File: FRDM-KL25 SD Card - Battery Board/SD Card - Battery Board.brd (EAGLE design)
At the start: 81.3 x 53.3 mm, 72 parts, among them J10 SSW-103-02-S-S, J11 SSW-102-02-S-S, J12 SSW-103-02-S-S, J13 SSW-103-02-S-S, J14 SSW-103-02-S-S, J3 SSW-108-02-S-D, J4 SSW-110-02-S-D, J5 SSW-108-02-S-D, J6 SSW-106-02-S-D, J7 SSW-102-02-S-S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

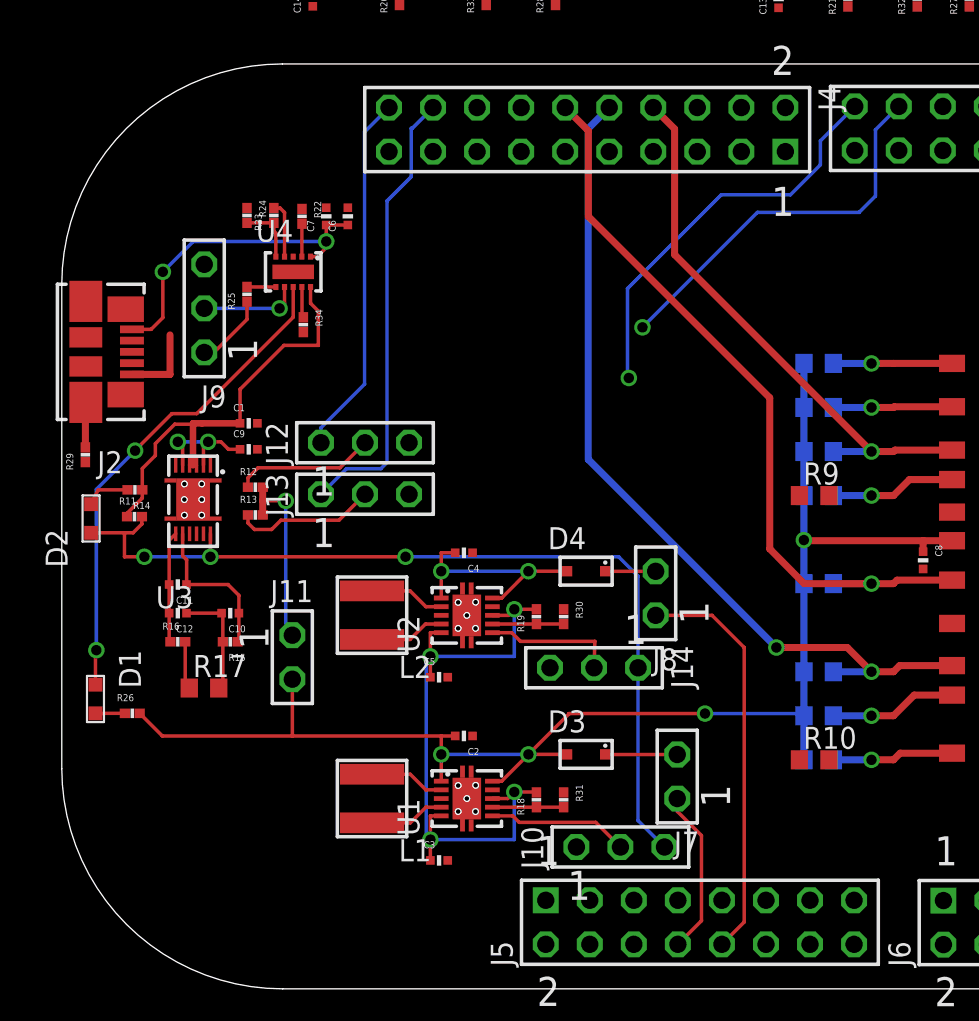
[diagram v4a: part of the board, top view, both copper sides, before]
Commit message: FRDM-KL25Z: Added a battery connector that uses a 1mm pitch. A few connections have been cleaned up to allow for better routing
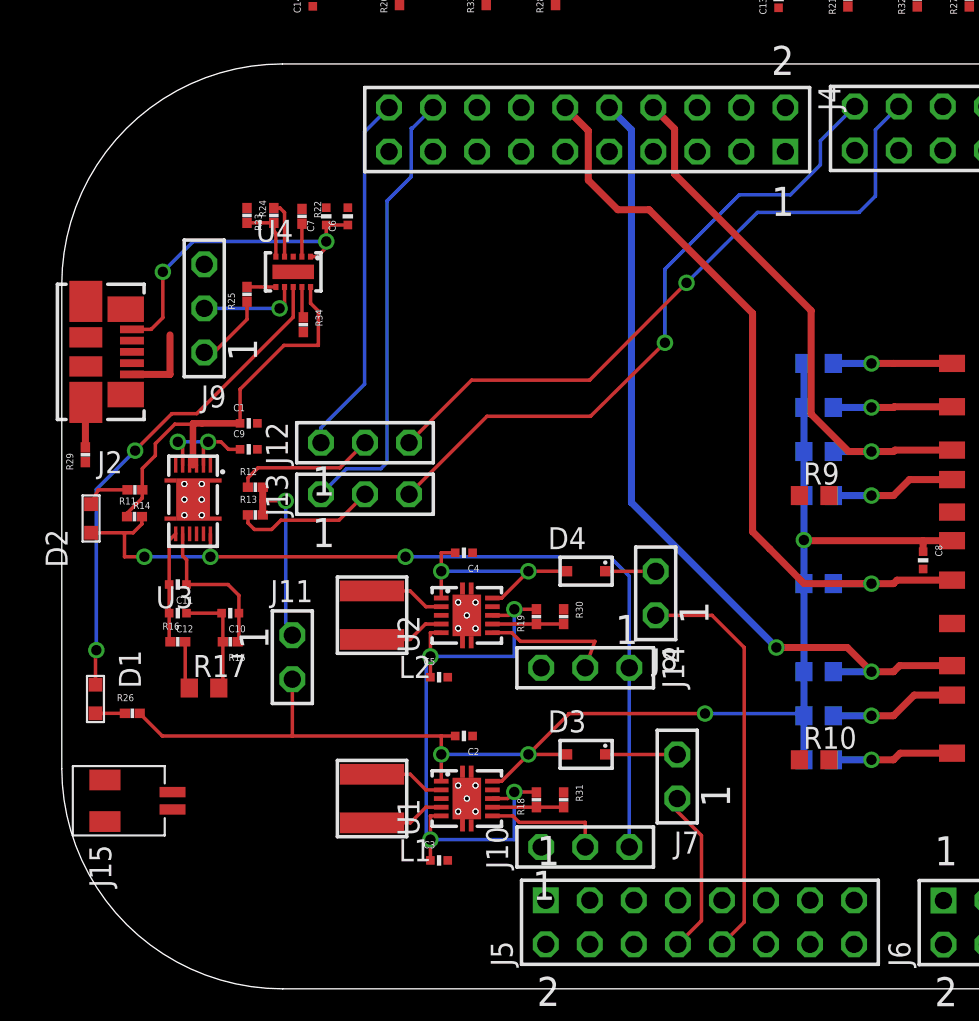
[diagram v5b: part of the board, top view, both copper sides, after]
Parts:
- added J15: 501568-0207-V2, Kas-Connectors:50156-0207
- moved J10 2.03 mm to (15.2, 5.36)
- moved J14 0.51 mm to (15.2, 15.7)
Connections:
- net PACK+: now also J15.P$1
- net PACK-: now also J15.P$2
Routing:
- net I2C-SCL-0: track 22.3 -> 38.5 mm
- net I2C-SDA-0: track 23.5 -> 38.3 mm
- net N$2: track 8.13 -> 6.93 mm
- net !BAT_LOW: track 52.6 -> 51.5 mm
- net SPI-SCLK-SD: track 44.0 -> 45.0 mm
- net SPI-MISO-SD: track 49.2 -> 48.2 mm
- net SPI-MOSI-SD: track 31.9 -> 32.7 mm

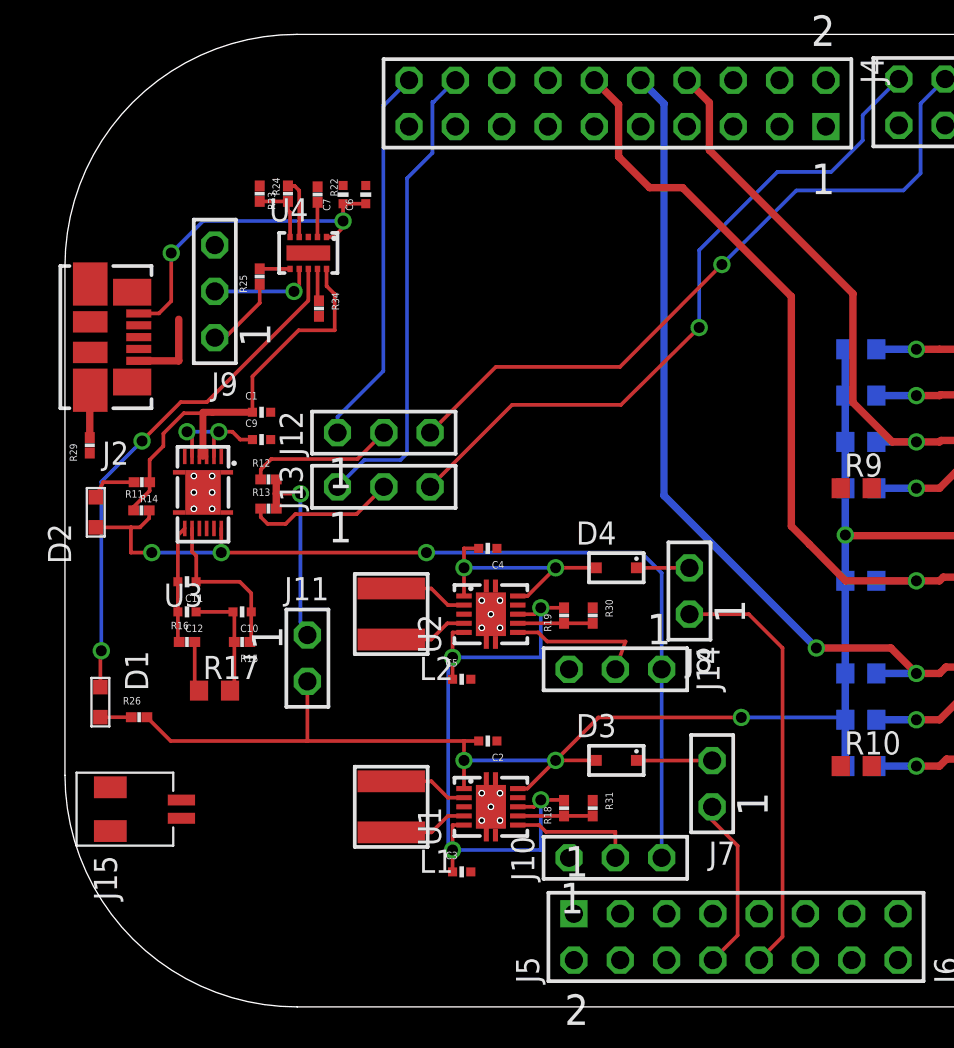
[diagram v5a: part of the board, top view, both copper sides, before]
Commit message: FRDM-KL25Z: All connections have been routed NOT cleanly. The board still needs cleaning up and this will hopefully be done before the next commit
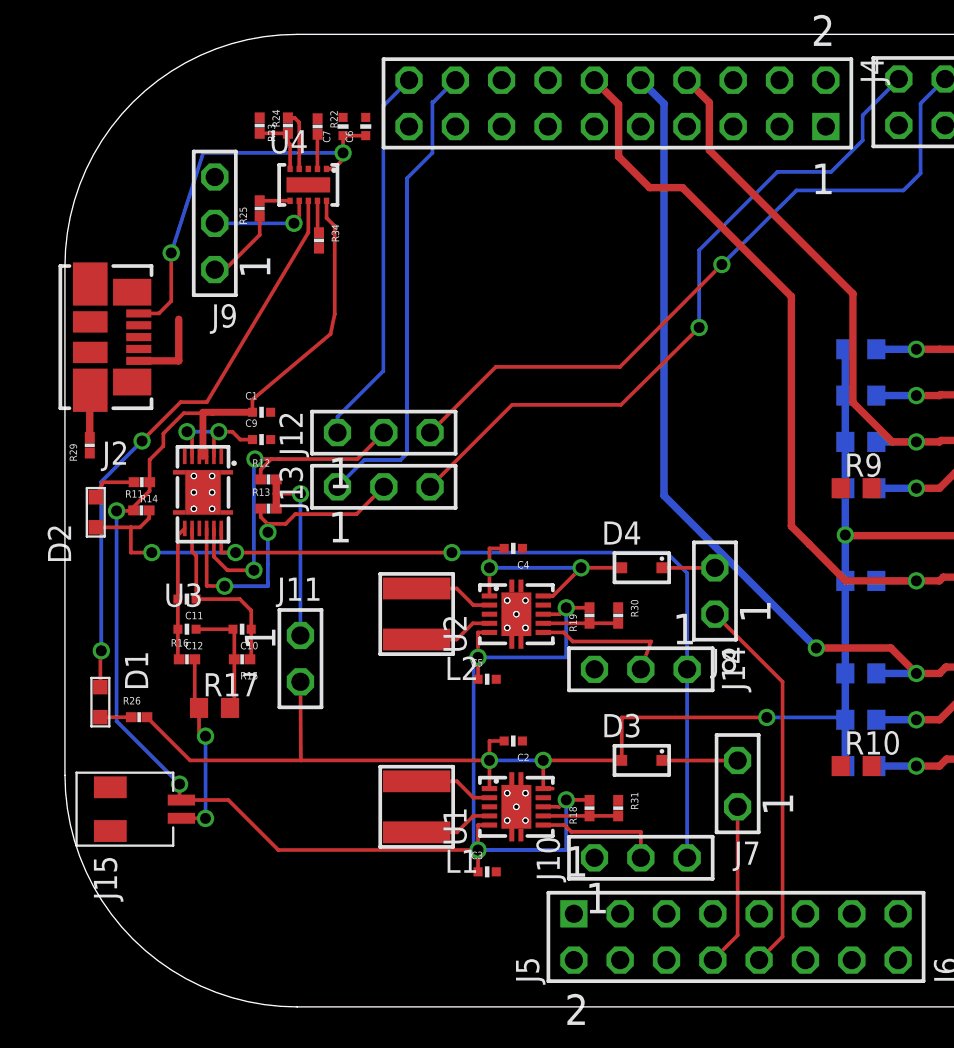
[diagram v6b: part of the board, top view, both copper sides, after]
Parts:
- moved C6 3.73 mm to (1.55, 45.5)
- moved C7 3.73 mm to (0.30, 45.5)
- moved J9 3.73 mm to (-6.73, 40.2)
- moved R22 3.73 mm to (-1.09, 45.5)
- moved R23 3.73 mm to (-2.72, 45.5)
- moved R24 3.73 mm to (-4.27, 45.5)
- moved U4 3.73 mm to (-1.60, 42.3)
- moved R25 3.73 mm to (-4.27, 41.0)
- moved R34 3.73 mm to (-1.02, 39.2)
- moved D3 1.40 mm to (16.7, 10.7)
- moved D4 1.40 mm to (16.7, 21.3)
- moved J8 1.40 mm to (20.7, 20.0)
- moved C2 1.40 mm to (9.64, 11.8)
- moved C3 1.40 mm to (8.21, 4.59)
- moved C4 1.40 mm to (9.64, 22.3)
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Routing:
- net PACK+: track 62.4 -> 100.8 mm, vias 4 -> 6
- net SCL: track 8.13 -> 19.2 mm, vias 0 -> 2
- net SDA: track 8.21 -> 18.1 mm, vias 0 -> 2
- net PACK-: track 2.76 -> 10.8 mm, vias 0 -> 2
- net +5V_CHARGE: track 18.5 -> 21.8 mm
- net !CHARGE: track 28.5 -> 31.5 mm
- net 5V_KL25Z: track 23.5 -> 21.0 mm
- net !BAT_LOW: track 51.5 -> 53.7 mm
- net N$6: track 6.46 -> 7.41 mm
- net N$7: track 9.06 -> 10.0 mm
- net 3.3V_KL25Z: track 9.55 -> 8.97 mm

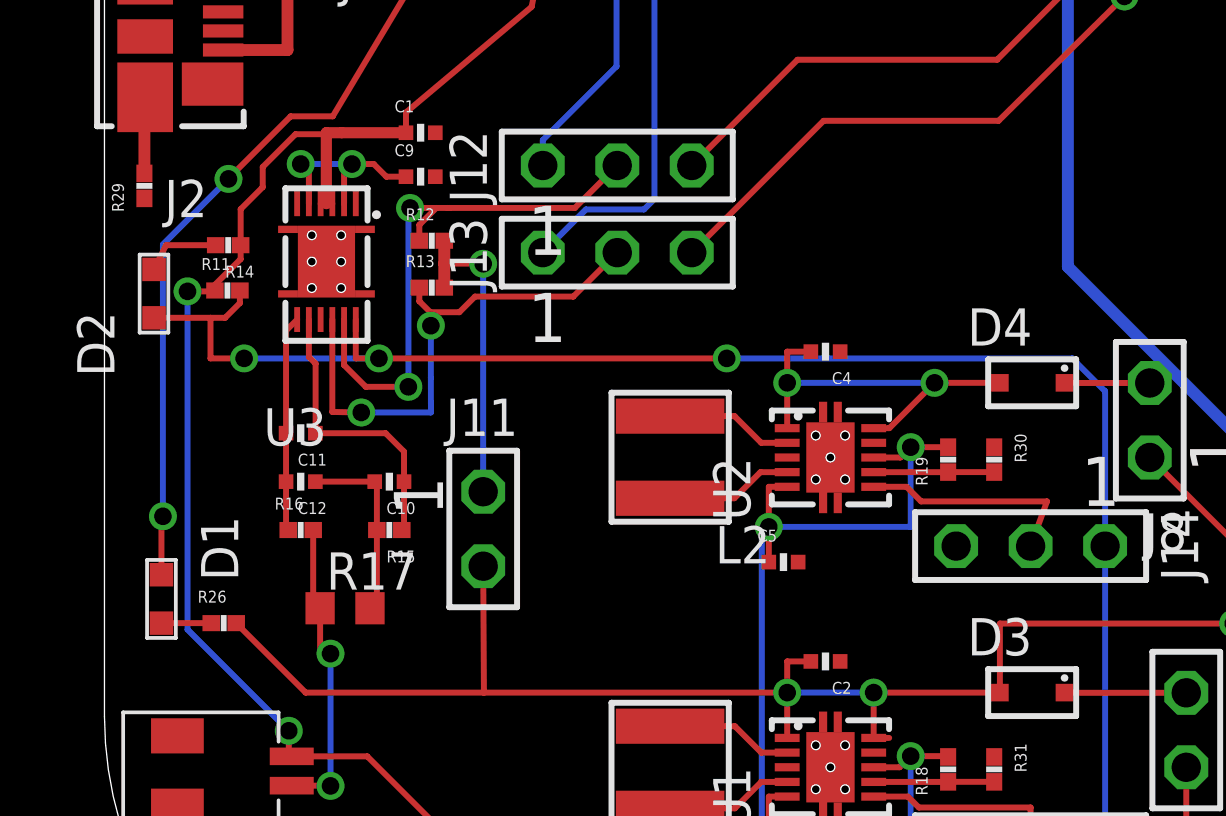
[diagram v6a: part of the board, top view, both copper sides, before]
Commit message: FRDM-KL25Z: Cleaned up a few routed connections
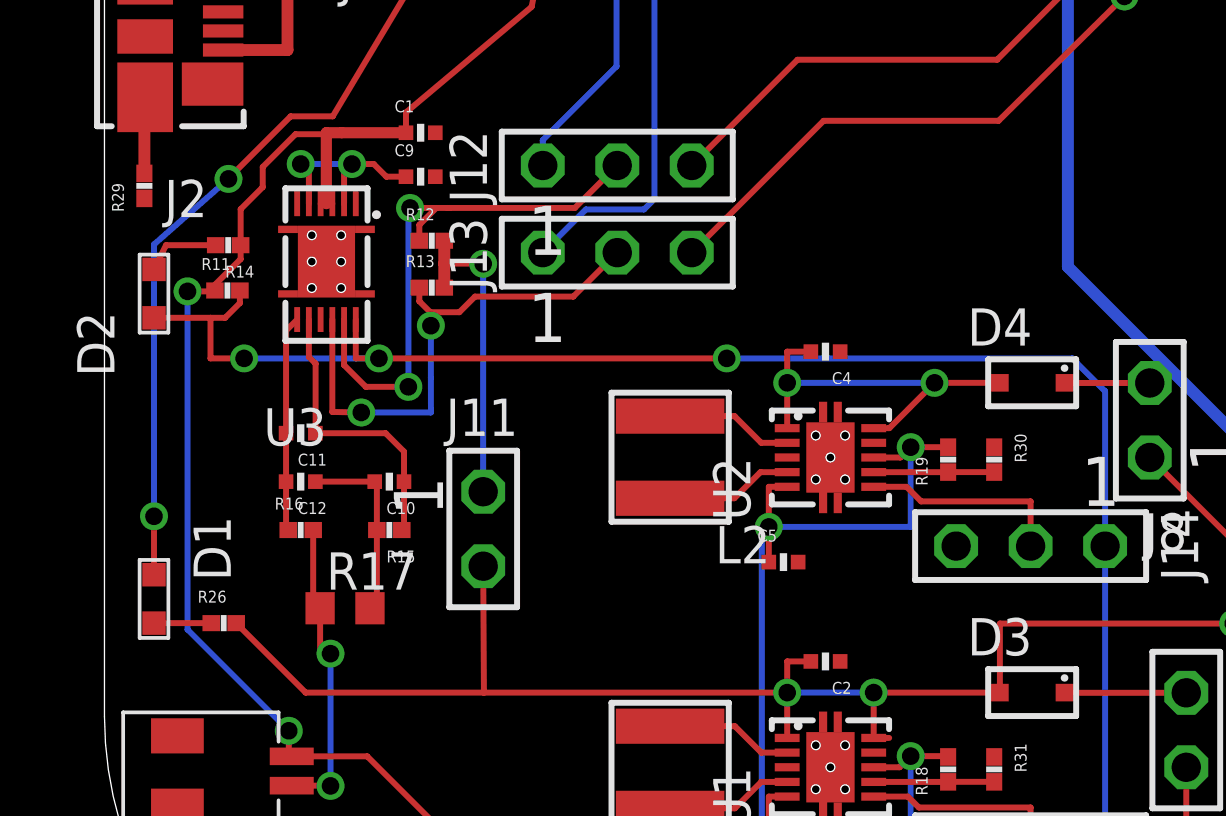
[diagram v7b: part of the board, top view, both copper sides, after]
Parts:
- moved D1 0.25 mm to (-13.3, 13.9)
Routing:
- net N$13: track 7.74 -> 7.08 mm
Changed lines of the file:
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@@
 <attribute name="POWER_RATING" value="63mW" x="-10.8812" y="13.0702" size="1.778" layer="27" display="off"/>
 </element>
-<element name="D1" library="Kas-Diodes-LEDs" package="0.8X1.2" value="Red-LED" x="-13.0048" y="13.8956" rot="R90">
-<attribute name="MANUFACTURER" value="Kingbright" x="27.6352" y="60.8856" size="1.778" layer="27" rot="R90" display="off"/>
-<attribute name="WAVELENGTH" value="470nm" x="27.6352" y="60.8856" size="1.778" layer="27" rot="R90" display="off"/>
-<attribute name="LUMINOUS_INTENSITY" value="95cmd" x="27.6352" y="60.8856" size="1.778" layer="27" rot="R90" display="off"/>
-<attribute name="NEWARK_PART_NUMBER" value="56P5113" x="27.6352" y="60.8856" size="1.778" layer="27" rot="R90" display="off"/>
-<attribute name="MANUFACTURER_PART_NUMBER" value="KPG-1608QBC-E" x="27.6352" y="60.8856" size="1.778" layer="27" rot="R90" display="off"/>
-<attribute name="COLOR" value="Blue" x="27.6352" y="60.8856" size="1.778" layer="27" rot="R90" display="off"/>
-<attribute name="FORWARD_CURRENT" value="20mA" x="-13.0048" y="13.8956" size="1.778" layer="27" rot="R90" display="off"/>
-<attribute name="VIEWING_ANGLE" value="120" x="-13.0048" y="13.8956" size="1.778" layer="27" rot="R90" display="off"/>
-<attribute name="FORWARD_VOLTAGE" value="3.3" x="-13.0048" y="13.8956" size="1.778" layer="27" rot="R90" display="off"/>
+<element name="D1" library="Kas-Diodes-LEDs" package="0.8X1.2" value="Red-LED" x="-13.2588" y="13.8956" rot="R90">
+<attribute name="MANUFACTURER" value="Kingbright" x="27.3812" y="60.8856" size="1.778" layer="27" rot="R90" display="off"/>
+<attribute name="WAVELENGTH" value="470nm" x="27.3812" y="60.8856" size="1.778" layer="27" rot="R90" display="off"/>
+<attribute name="LUMINOUS_INTENSITY" value="95cmd" x="27.3812" y="60.8856" size="1.778" layer="27" rot="R90" display="off"/>
+<attribute name="NEWARK_PART_NUMBER" value="56P5113" x="27.3812" y="60.8856" size="1.778" layer="27" rot="R90" display="off"/>
+<attribute name="MANUFACTURER_PART_NUMBER" value="KPG-1608QBC-E" x="27.3812" y="60.8856" size="1.778" layer="27" rot="R90" display="off"/>
+<attribute name="COLOR" value="Blue" x="27.3812" y="60.8856" size="1.778" layer="27" rot="R90" display="off"/>
+<attribute name="FORWARD_CURRENT" value="20mA" x="-13.2588" y="13.8956" size="1.778" layer="27" rot="R90" display="off"/>
+<attribute name="VIEWING_ANGLE" value="120" x="-13.2588" y="13.8956" size="1.778" layer="27" rot="R90" display="off"/>
+<attribute name="FORWARD_VOLTAGE" value="3.3" x="-13.2588" y="13.8956" size="1.778" layer="27" rot="R90" display="off"/>
 </element>
 <element name="J1" library="Kas-Connectors" package="693061010911" value="" x="60.706" y="23.8506">
@@
 <wire x1="-10.7188" y1="28.2334" x2="-10.7188" y2="28.2194" width="0.2032" layer="1"/>
 <via x="-10.7188" y="28.2194" extent="1-16" drill="0.6"/>
-<wire x1="-10.7188" y1="28.2194" x2="-12.954" y2="25.9842" width="0.2032" layer="16"/>
-<wire x1="-12.954" y1="25.9842" x2="-12.954" y2="16.7132" width="0.2032" layer="16"/>
-<via x="-12.954" y="16.7132" extent="1-16" drill="0.6"/>
-<wire x1="-12.954" y1="16.7132" x2="-13.0048" y2="16.6624" width="0.2032" layer="1"/>
-<wire x1="-13.0048" y1="16.6624" x2="-13.0048" y2="14.7206" width="0.2032" layer="1"/>
+<wire x1="-10.7188" y1="28.2194" x2="-13.2588" y2="25.9842" width="0.2032" layer="16"/>
+<wire x1="-13.2588" y1="25.9842" x2="-13.2588" y2="16.7132" width="0.2032" layer="16"/>
+<via x="-13.2588" y="16.7132" extent="1-16" drill="0.6"/>
+<wire x1="-13.2588" y1="16.7132" x2="-13.2588" y2="14.7206" width="0.2032" layer="1"/>
 </signal>
 <signal name="N$10">
 <contactref element="D1" pad="P$1"/>
 <contactref element="R26" pad="1"/>
-<wire x1="-13.0048" y1="13.0706" x2="-13.0044" y2="13.0702" width="0.2032" layer="1"/>
+<wire x1="-13.2588" y1="13.0706" x2="-13.0044" y2="13.0702" width="0.2032" layer="1"/>
 <wire x1="-13.0044" y1="13.0702" x2="-11.3062" y2="13.0702" width="0.2032" layer="1"/>
 </signal>
@@
 <contactref element="U2" pad="P$6"/>
 <contactref element="J14" pad="2"/>
-<wire x1="16.637" y1="15.6972" x2="17.1958" y2="17.2212" width="0.2032" layer="1"/>
-<wire x1="17.1958" y1="17.2212" x2="12.9032" y2="17.2212" width="0.2032" layer="1"/>
+<wire x1="16.637" y1="15.6972" x2="16.637" y2="17.2212" width="0.2032" layer="1"/>
+<wire x1="16.637" y1="17.2212" x2="12.9032" y2="17.2212" width="0.2032" layer="1"/>
 <wire x1="12.9032" y1="17.2212" x2="12.4054" y2="17.719" width="0.2032" layer="1"/>
 <wire x1="12.4054" y1="17.719" x2="11.2854" y2="17.719" width="0.2032" layer="1"/>
